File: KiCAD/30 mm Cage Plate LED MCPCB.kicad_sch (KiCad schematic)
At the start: 22 parts, among them IC1 AL8843QSP-13, J1 Conn_01x08_Socket, U2 TLP3480, U3 TLP3480, U4 TLP3480, U5 TLP3480

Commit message: Before adding mux to PCB
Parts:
- C1, C2, C3: value 10μF -> 22μF; footprint Capacitor_SMD:C_0603_1608Metric -> Capacitor_SMD:C_0805_2012Metric; Manufacturer Murata Electronics -> Samsung Electro-Mechanics; Part GRM188R6YA106MA73D -> CL21A226MAYNNNE

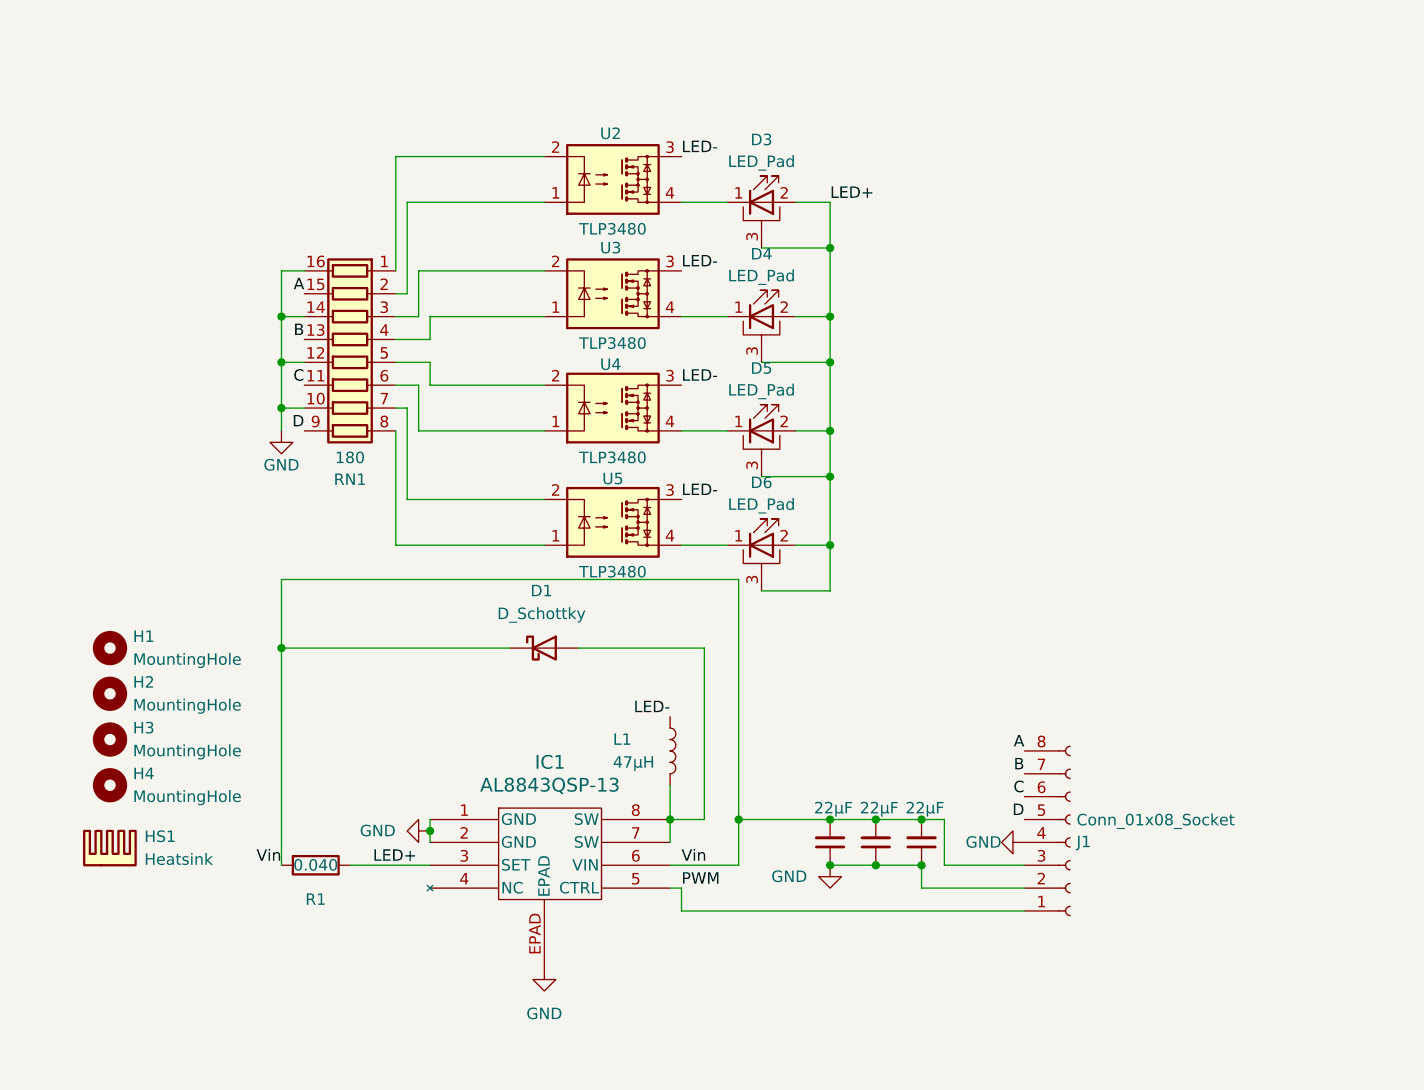
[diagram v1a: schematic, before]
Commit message: Fan added
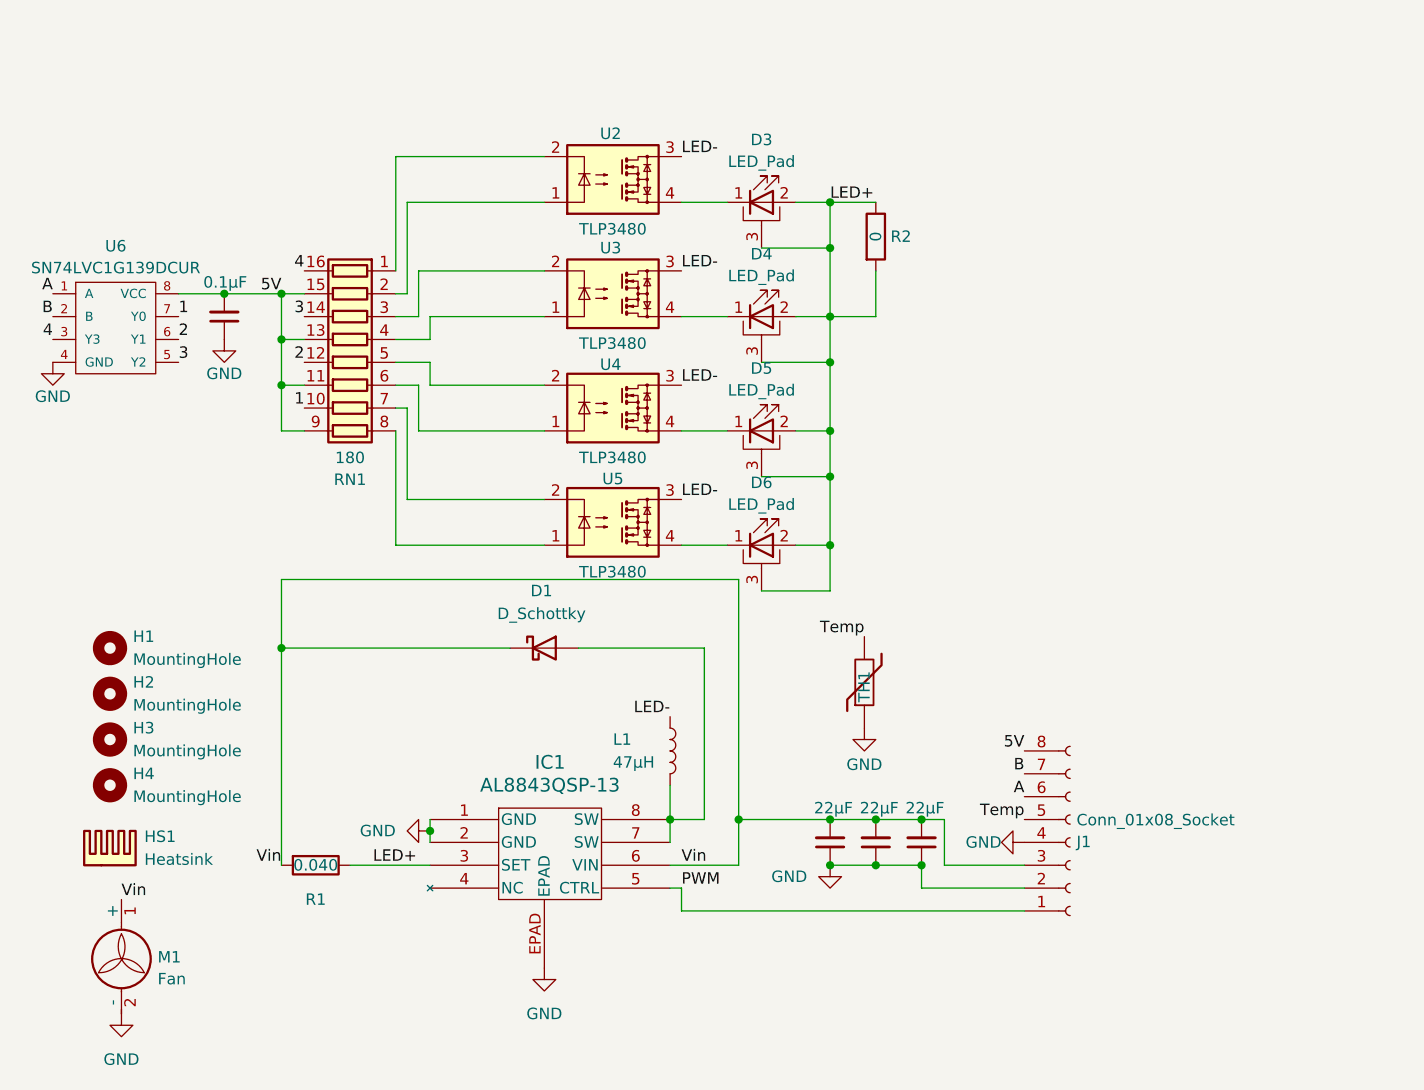
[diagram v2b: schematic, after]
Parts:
- added C4: 0.1μF, Capacitor_SMD:C_0603_1608Metric, symbol Device:C_Small
- added M1: Fan, symbol Motor:Fan
- added R2: 0, Resistor_SMD:R_1206_3216Metric, symbol Device:R
- added TH1: Thermistor, Resistor_SMD:R_0603_1608Metric, symbol Device:Thermistor
- added U6: SN74LVC1G139DCUR, Custom:SOP50P310X90-8N, symbol Custom:SN74LVC1G139DCUR
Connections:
- net A: now also J1.6 (Pin_6), U6.1 (A); no longer J1.8 (Pin_8), RN1.15 (R2.2)
- net B: now also U6.2 (B); no longer RN1.13 (R4.2)
- net GND: now also C4.1, M1.2 (-), TH1.1, U6.4 (GND); no longer RN1.10 (R7.2), RN1.12 (R5.2), RN1.14 (R3.2), RN1.16 (R1.2)
- net LED+: now also R2.1, R2.2
- net Vin: now also M1.1 (+)
- net C renamed 5V
- net 5V: now also J1.8 (Pin_8), RN1.13 (R4.2), RN1.15 (R2.2), RN1.9 (R8.2), C4.2, U6.8 (VCC); no longer J1.6 (Pin_6)
- net D renamed Temp
- net Temp: now also TH1.2; no longer RN1.9 (R8.2)
- new net 1: RN1.10 (R7.2), U6.7 (Y0)
- new net 2: RN1.12 (R5.2), U6.6 (Y1)
- new net 3: RN1.14 (R3.2), U6.5 (Y2)
- new net 4: RN1.16 (R1.2), U6.3 (Y3)

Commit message: More copper for LEDs, OSHW logo
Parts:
- renumbered R2 to J2
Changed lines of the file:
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@@
 		(on_board yes)
 		(dnp no)
-		(property "Reference" "R2"
+		(property "Reference" "J2"
 			(at 181.864 41.91 0)
 			(effects
@@
 			(project "30 mm Cage Plate LED MCPCB"
 				(path "/d4bfa918-6f2d-41e7-978b-b2160bded453"
-					(reference "R2")
+					(reference "J2")
 					(unit 1)
 				)
@@
 					(unit 1)
 				)
+			)
+		)
+	)
+	(symbol
+		(lib_id "Graphic:Logo_Open_Hardware_Small")
+		(at 97.79 72.39 0)
+		(unit 1)
+		(exclude_from_sim no)
+		(in_bom no)
+		(on_board no)
+		(dnp no)
+		(fields_autoplaced yes)
+		(property "Reference" "#SYM1"
+			(at 97.79 65.405 0)
+			(effects
+				(font
+					(size 1.27 1.27)
+				)
+				(hide yes)
+			)
+		)
+		(property "Value" "Logo_Open_Hardware_Small"
+			(at 97.79 78.105 0)
+			(effects
+				(font
+					(size 1.27 1.27)
+				)
+				(hide yes)
+			)
+		)
+		(property "Footprint" ""
+			(at 97.79 72.39 0)
+			(effects
+				(font
+					(size 1.27 1.27)
+				)
+				(hide yes)
+			)
+		)
+		(property "Datasheet" "~"
+			(at 97.79 72.39 0)
+			(effects
+				(font
+					(size 1.27 1.27)
+				)
+				(hide yes)
+			)
+		)
+		(property "Description" "Open Hardware logo, small"
+			(at 97.79 72.39 0)
+			(effects
+				(font
+					(size 1.27 1.27)
+				)
+				(hide yes)
+			)
+		)
+		(property "Sim.Enable" "0"
+			(at 97.79 72.39 0)
+			(effects
+				(font
+					(size 1.27 1.27)
+				)
+				(hide yes)
+			)
+		)
+		(instances
+			(project ""
+				(path "/d4bfa918-6f2d-41e7-978b-b2160bded453"
+					(reference "#SYM1")
+					(unit 1)
+				)

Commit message: update
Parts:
- added SYM1: Logo_Open_Hardware_Small, Symbol:OSHW-Logo_5.7x6mm_SilkScreen, symbol Graphic:Logo_Open_Hardware_Small
- added SYM2: Logo_Open_Hardware_Small, Custom:CC-BY-SA Symbol, symbol Graphic:Logo_Open_Hardware_Small
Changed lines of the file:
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@@
+	)
+	(symbol
+		(lib_id "Graphic:Logo_Open_Hardware_Small")
+		(at 97.79 72.39 0)
+		(unit 1)
+		(exclude_from_sim yes)
+		(in_bom no)
+		(on_board yes)
+		(dnp no)
+		(fields_autoplaced yes)
+		(property "Reference" "SYM2"
+			(at 97.79 65.405 0)
+			(effects
+				(font
+					(size 1.27 1.27)
+				)
+				(hide yes)
+			)
+		)
+		(property "Value" "Logo_Open_Hardware_Small"
+			(at 97.79 78.105 0)
+			(effects
+				(font
+					(size 1.27 1.27)
+				)
+				(hide yes)
+			)
+		)
+		(property "Footprint" "Custom:CC-BY-SA Symbol"
+			(at 97.79 72.39 0)
+			(effects
+				(font
+					(size 1.27 1.27)
+				)
+				(hide yes)
+			)
+		)
+		(property "Datasheet" "~"
+			(at 97.79 72.39 0)
+			(effects
+				(font
+					(size 1.27 1.27)
+				)
+				(hide yes)
+			)
+		)
+		(property "Description" "Open Hardware logo, small"
+			(at 97.79 72.39 0)
+			(effects
+				(font
+					(size 1.27 1.27)
+				)
+				(hide yes)
+			)
+		)
+		(property "Manufacturer" ""
+			(at 97.79 72.39 0)
+			(effects
+				(font
+					(size 1.27 1.27)
+				)
+				(hide yes)
+			)
+		)
+		(property "Part" ""
+			(at 97.79 72.39 0)
+			(effects
+				(font
+					(size 1.27 1.27)
+				)
+				(hide yes)
+			)
+		)
+		(instances
+			(project "30 mm Cage Plate LED MCPCB"
+				(path "/d4bfa918-6f2d-41e7-978b-b2160bded453"
+					(reference "SYM2")
+					(unit 1)
+				)
+			)
+		)
 	)
 	(symbol
@@
 		(at 97.79 72.39 0)
 		(unit 1)
-		(exclude_from_sim no)
+		(exclude_from_sim yes)
 		(in_bom no)
-		(on_board no)
+		(on_board yes)
 		(dnp no)
 		(fields_autoplaced yes)
-		(property "Reference" "#SYM1"
+		(property "Reference" "SYM1"
 			(at 97.79 65.405 0)
 			(effects
@@
 			)
 		)
-		(property "Footprint" ""
+		(property "Footprint" "Symbol:OSHW-Logo_5.7x6mm_SilkScreen"
 			(at 97.79 72.39 0)
 			(effects
@@
 			)
 		)
-		(property "Sim.Enable" "0"
+		(property "Manufacturer" ""
 			(at 97.79 72.39 0)
 			(effects
@@
 			)
 		)
+		(property "Part" ""
+			(at 97.79 72.39 0)
+			(effects
+				(font
+					(size 1.27 1.27)
+				)
+				(hide yes)
+			)
+		)
 		(instances
 			(project ""
 				(path "/d4bfa918-6f2d-41e7-978b-b2160bded453"
-					(reference "#SYM1")
-					(unit 1)
-				)
+					(reference "SYM1")
+					(unit 1)
+				)

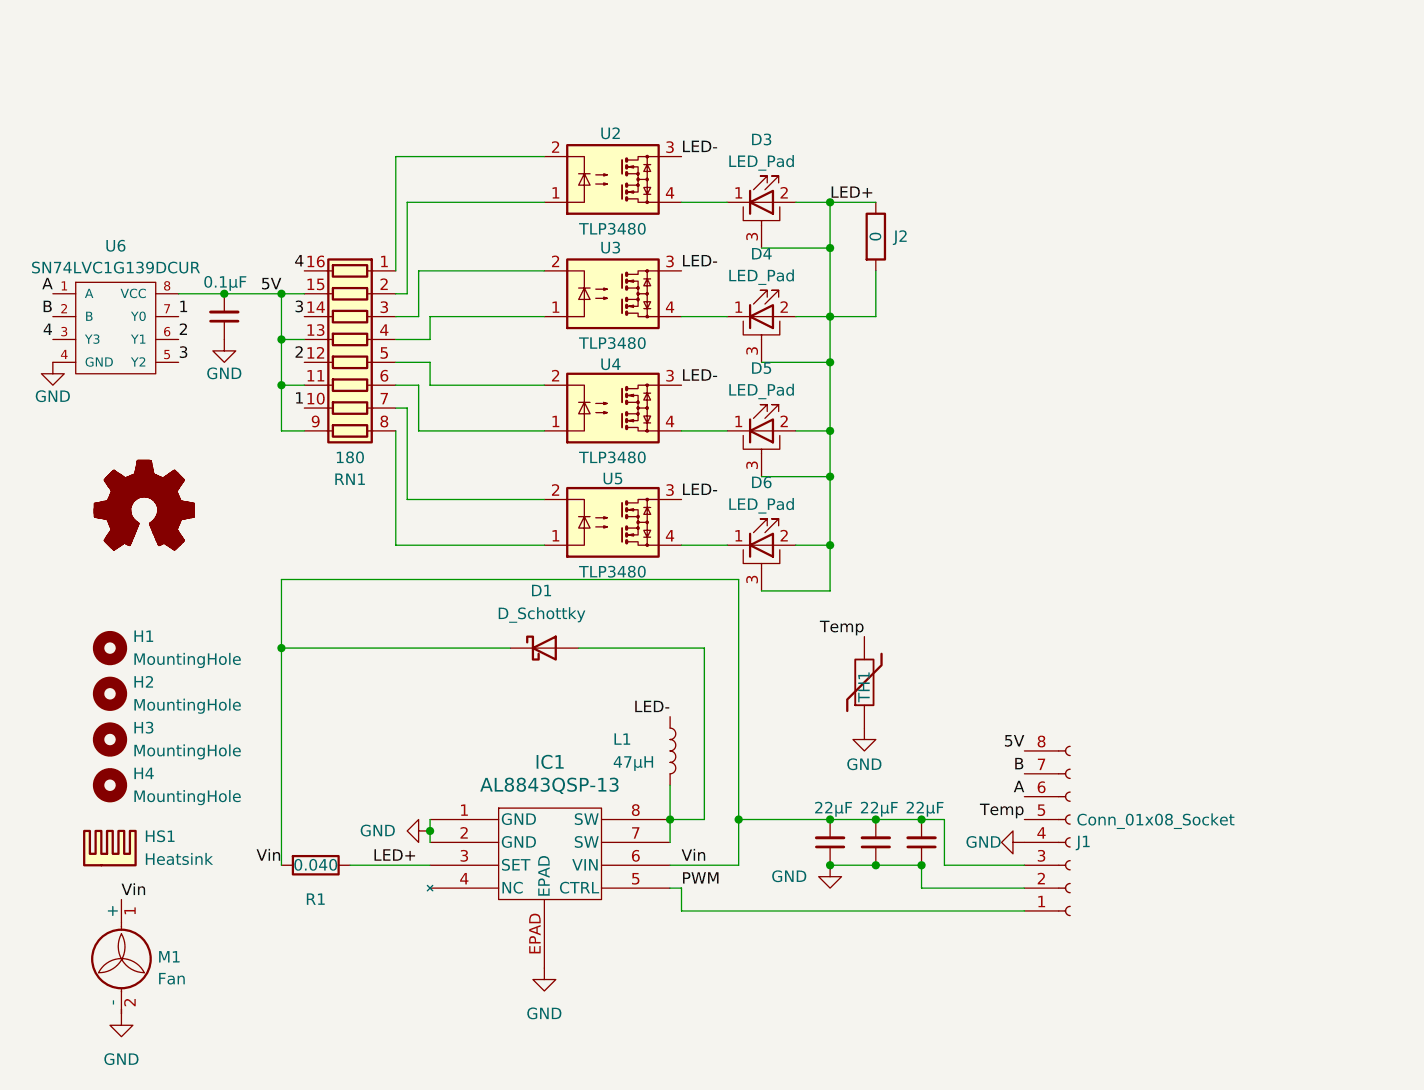
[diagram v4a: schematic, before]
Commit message: Add pmos array mux
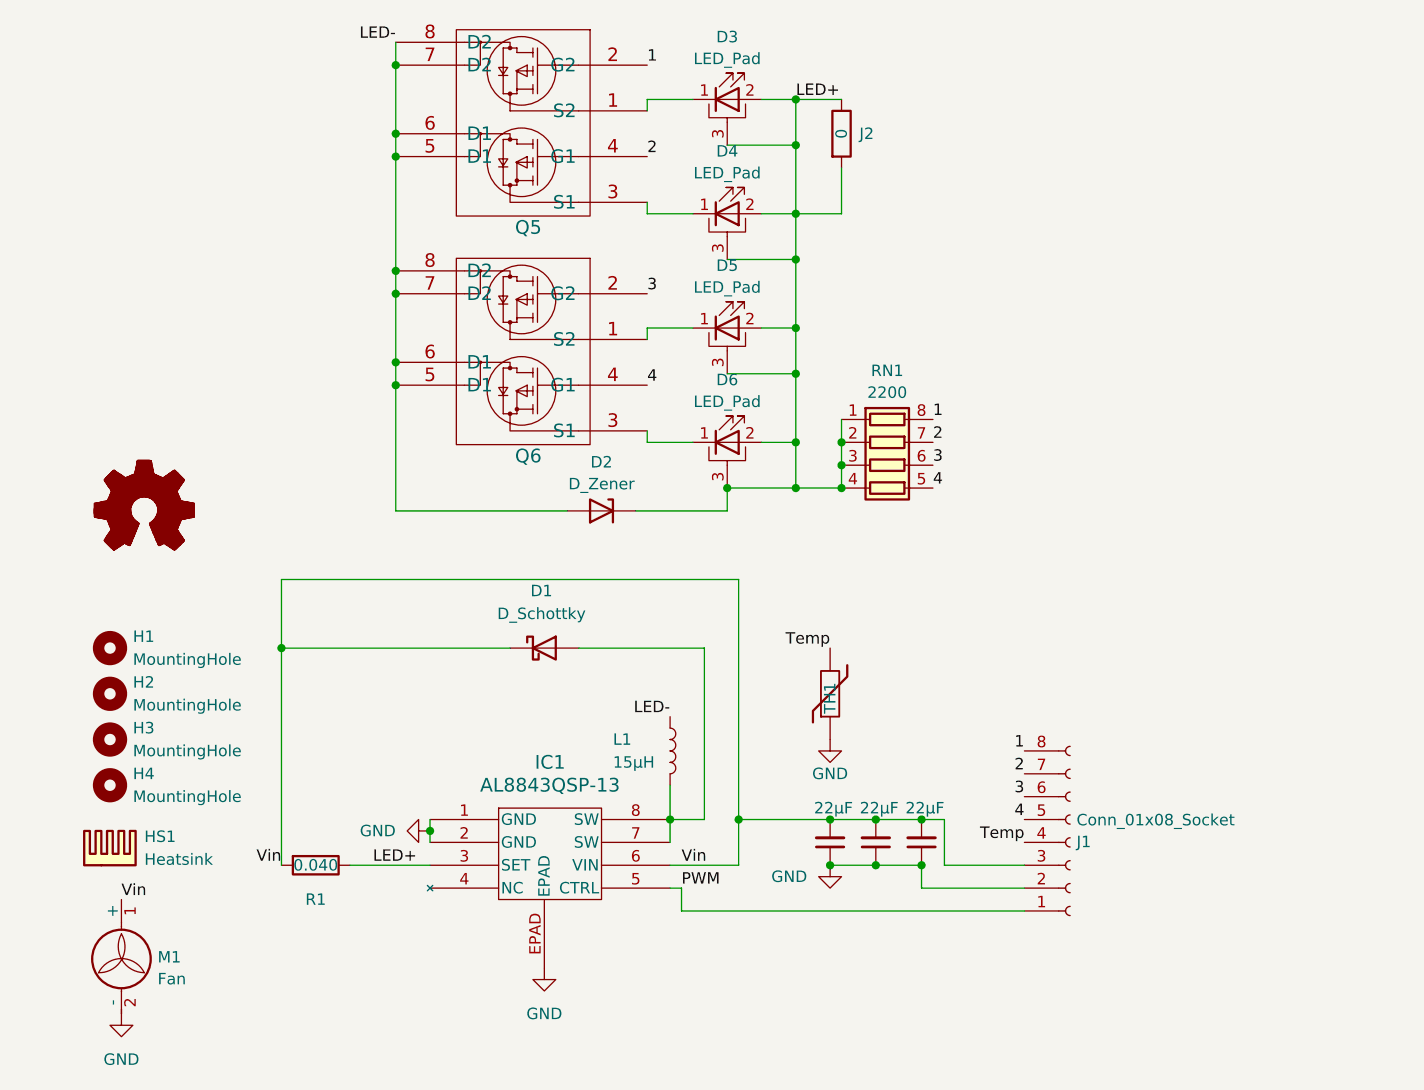
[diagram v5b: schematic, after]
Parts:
- removed C4: 0.1μF, Capacitor_SMD:C_0603_1608Metric, symbol Device:C_Small
- removed RN1: 180, Resistor_SMD:R_Array_Convex_8x0602, symbol Device:R_Pack08
- removed U2, U3, U4, U5: TLP3480, Custom:TLP3480-SSR, symbol Relay_SolidState:ASSR-1218
- removed U6: SN74LVC1G139DCUR, Custom:SOP50P310X90-8N, symbol Custom:SN74LVC1G139DCUR
- added D2: D_Zener, Custom:DFN6_TDS3011_SEM, symbol Device:D_Zener
- added Q5, Q6: 2x_p-channel, Custom:SOP-8_3.9x4.9mm_P1.27mm, symbol LED Driver 1x8 Mux-rescue:IRF9358TRPBF-2x_p-channel-Custom_parts
- added RN1: 2200, Resistor_SMD:R_Array_Convex_4x0603, symbol Device:R_Pack04
- L1: value 47μH -> 15μH; Part SRP1038A-470M -> SRP1038A-150M
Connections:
- net 5V is gone; now on net 1: J1.8 (Pin_8)
- net A is gone; now on net 3: J1.6 (Pin_6)
- net B is gone; now on net 2: J1.7 (Pin_7)
- net 1: now also Q5.2 (G2), RN1.8 (R1.2)
- net 2: now also Q5.4 (G1), RN1.7 (R2.2)
- net 3: now also Q6.2 (G2), RN1.6 (R3.2)
- net 4: now also J1.5 (Pin_5), Q6.4 (G1), RN1.5 (R4.2)
- net GND: no longer J1.4 (Pin_4)
- net LED+: now also D2.1 (K), RN1.1 (R1.1), RN1.2 (R2.1), RN1.3 (R3.1), RN1.4 (R4.1)
- net LED-: now also D2.2 (A), Q5.5 (D1), Q5.6 (D1), Q5.7 (D2), Q5.8 (D2), Q6.5 (D1), Q6.6 (D1), Q6.7 (D2), Q6.8 (D2)
- net Temp: now also J1.4 (Pin_4); no longer J1.5 (Pin_5)
- net at D6.1 (K): now also Q6.3 (S1)
- net at D4.1 (K): now also Q5.3 (S1)
- net at D5.1 (K): now also Q6.1 (S2)
- net at D3.1 (K): now also Q5.1 (S2)
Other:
- moved on the sheet: D3, D4, D5, D6, J2, TH1
